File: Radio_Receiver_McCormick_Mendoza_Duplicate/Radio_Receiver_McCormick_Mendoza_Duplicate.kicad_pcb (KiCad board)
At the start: 4 copper layers, 100 x 100 mm, 244 parts, among them J1 VBAT, J10 CLK_2, J11 I_LO, J12 Q_LO, J13 I_0, J14 I_180, J15 Q_90, J16 Q_270, J17 I_RAW, J18 Conn_01x02_Female, J19 Conn_01x02_Female, J2 GND, J20 Q_RAW, J21 SDR Out, J23 VDDA, J24 CLK_0, J25 OLED, J26 +5V, J28 Conn_01x01_Pin, J3 VA_3.3, J33 XFIL_IN, J34 XFIL_OUT, J35 3.5mm_Jack, J36 +5V RAW, J37 V_4.5, J38 DAC_FLT, J39 VDD, J4 VA_4.5, J40 DAC_FMT, J41 V_DIV, J42 VDDA/2, J45 CENTER_TAP, J46 3.5mm_Jack, J47 FIL_IN, J5 Conn_Coaxial, J6 Conn_01x02, J7 Micro_SD-TF_PUSH, J8 FIL_OUT, J9 CLK_1, SW1 RotaryEncoder_Switch_MP, SW6 09.03290.01, T1 Transformer_1P_SS, U1 TPS7A2045PDQN, U10 OPA1612AID, U11 INA821ID, U12 PCM1808PWR, U13 SN74CBT3253CDBR, U14 PCM5102A, U2 TPS7A2045PDQN, U3 TPS72733DSER, U4 Pico, U5 Si5351A-B-GT, U6 SN74AC74DR, U8 SN74CBT3253CDBR, U9 INA821ID, Y1 ASTX-H11-24.576MHZ-T

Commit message: Added comment
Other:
- board text added: "These is clustered by groups as shown in the Schematics. NOT FINISHED"
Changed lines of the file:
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@@
 		(layer "User.4")
+	)
+	(gr_text "These is clustered by groups as shown in the Schematics. \nNOT FINISHED\n"
+		(at -138 111.5 0)
+		(layer "F.Cu")
+		(effects
+			(font
+				(size 1.5 1.5)
+				(thickness 0.3)
+				(bold yes)
+			)
+			(justify left bottom)
+		)
 	)
 	(gr_text "Analog"

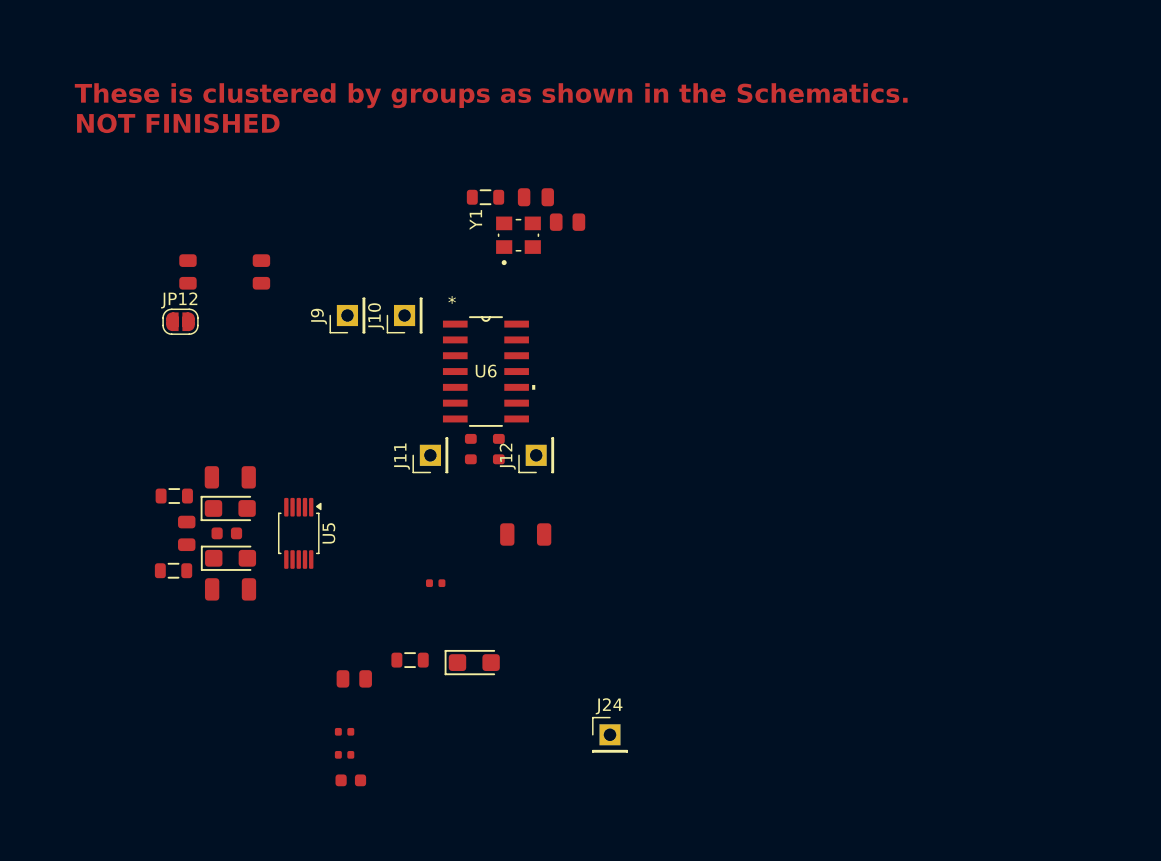
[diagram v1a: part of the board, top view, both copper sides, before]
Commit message: Fixed the clock and johnson counter
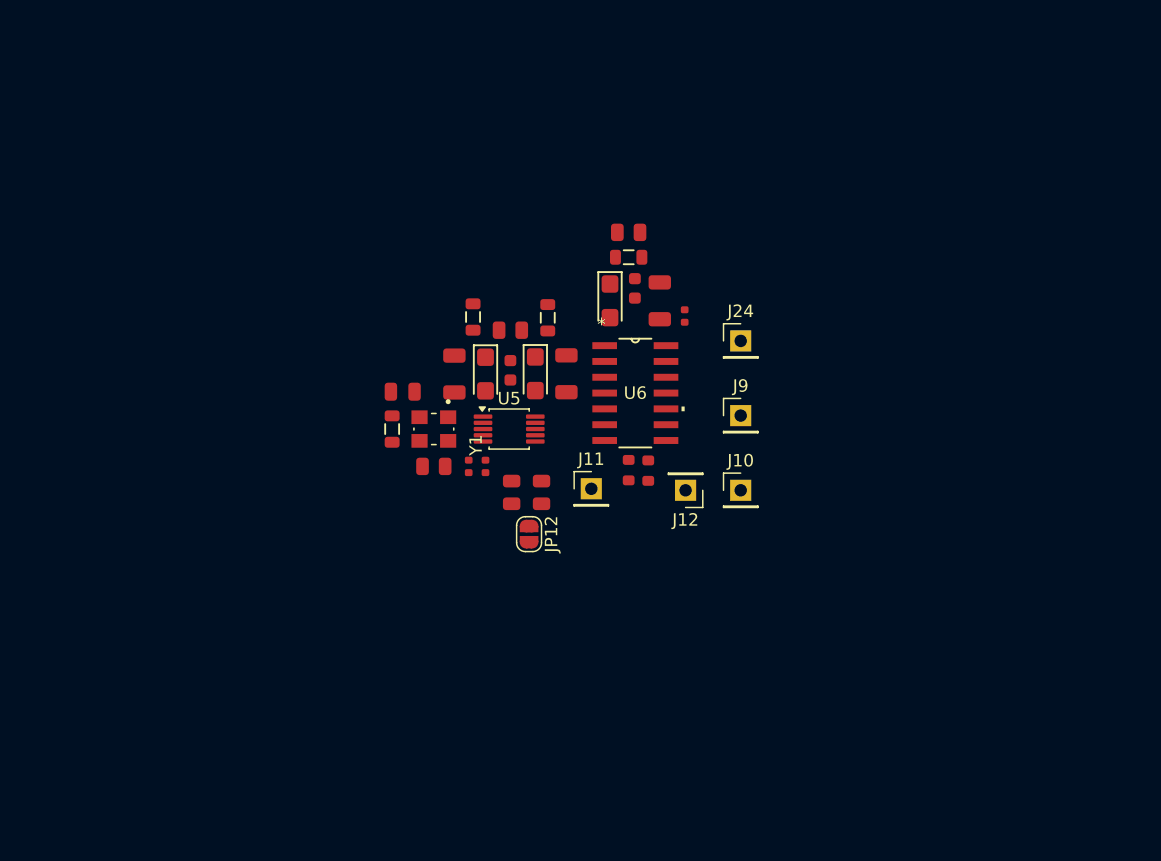
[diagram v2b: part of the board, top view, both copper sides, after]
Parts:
- moved C70 45.6 mm to (-93.0, 123.8), turned to -90 degrees
- moved R41 42.1 mm to (-93.5, 119.3)
- moved FB13 36.8 mm to (-93.5, 121.3)
- moved J24 33.3 mm to (-84.5, 128.0)
- moved FB15 33.2 mm to (-100.0, 126.2), turned to -90 degrees
- moved JP12 32.8 mm to (-101.5, 143.6), turned to -90 degrees
- moved J9 32.6 mm to (-84.5, 134.0), turned to 0 degrees
- moved FB16 31.5 mm to (-106.0, 126.1), turned to -90 degrees
- moved R36 31.5 mm to (-102.9, 140.2)
- moved C71 31.0 mm to (-95.0, 124.8), turned to -90 degrees
- moved R4 30.7 mm to (-103.0, 127.2), turned to 180 degrees
- moved J10 30.4 mm to (-84.5, 140.0), turned to 0 degrees
- moved C8 29.3 mm to (-89.0, 126.0), turned to 90 degrees
- moved R34 28.6 mm to (-100.5, 140.2)
- moved C77 28.3 mm to (-98.5, 130.7), turned to -90 degrees
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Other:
- board text removed: "These is clustered by groups as shown in the Schematics. NOT FINISHED"

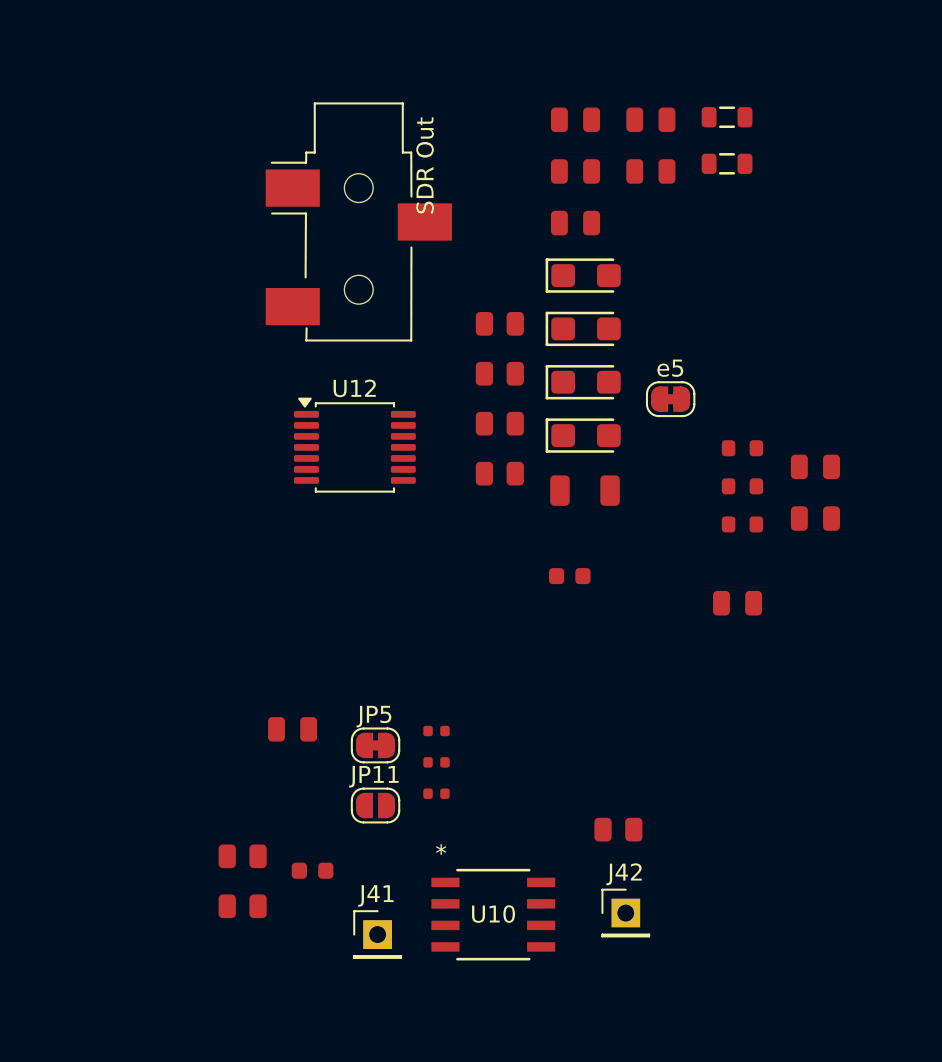
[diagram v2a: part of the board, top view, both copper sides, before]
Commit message: ADC finished
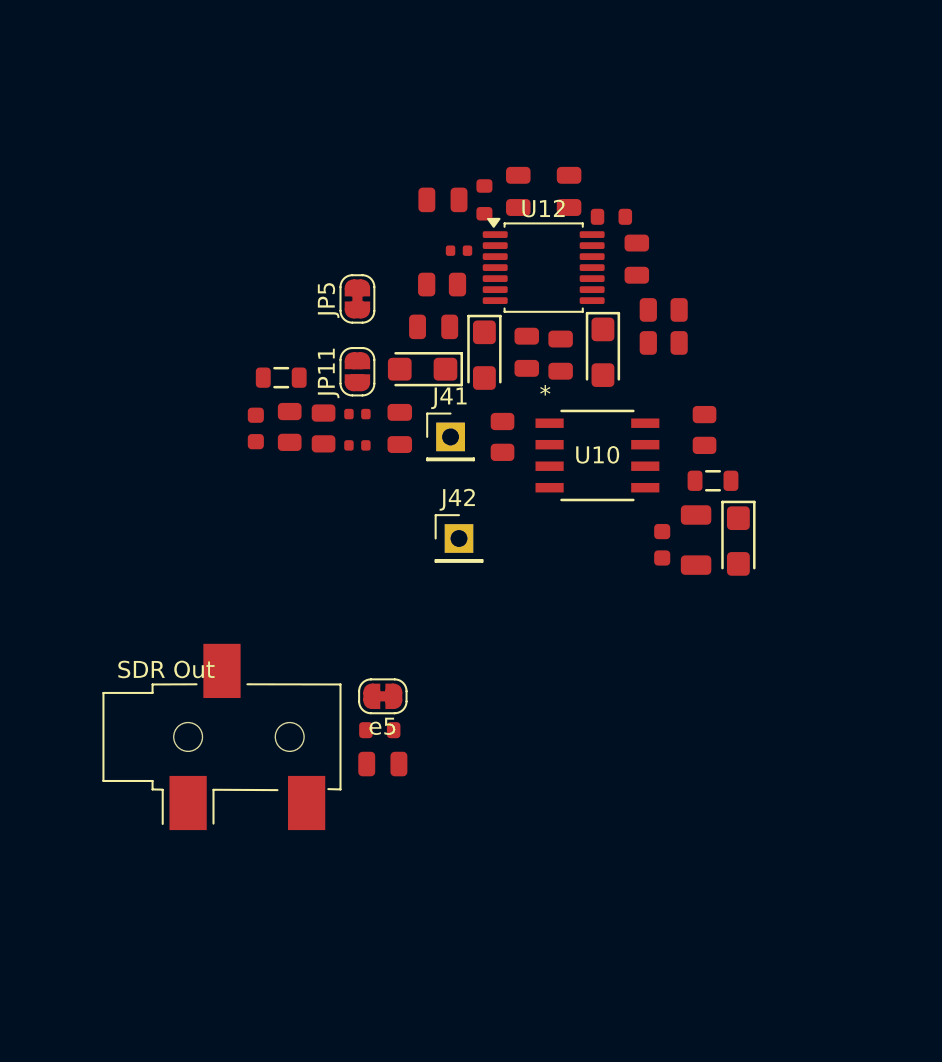
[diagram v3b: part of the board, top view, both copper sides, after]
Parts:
- moved R3 32.1 mm to (-25.0, 193.2), turned to 180 degrees
- moved J41 29.7 mm to (-25.5, 204.2)
- moved FB21 29.2 mm to (-35.5, 200.7)
- moved J21 29.1 mm to (-37.0, 221.9), turned to 90 degrees
- moved R53 28.6 mm to (-33.0, 203.7), turned to -90 degrees
- moved U10 27.8 mm to (-16.8, 205.3)
- moved C23 27.1 mm to (-25.9, 190.2), turned to 180 degrees
- moved JP5 26.4 mm to (-31.0, 196.0), turned to 90 degrees
- moved C93 26.3 mm to (-37.0, 203.7), turned to -90 degrees
- moved JP11 25.6 mm to (-31.0, 200.3), turned to 90 degrees
- moved R52 25.5 mm to (-35.0, 203.6), turned to -90 degrees
- moved R31 24.6 mm to (-29.7, 221.5)
- moved e5 24.4 mm to (-29.5, 219.5), turned to 180 degrees
- moved J42 24.2 mm to (-25.0, 210.2)
- moved R5 24.2 mm to (-22.4, 204.2), turned to 90 degrees
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
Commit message: Started adding traces
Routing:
- net GND: track 0.00 -> 78.4 mm
- net V_DIV: track 0.00 -> 12.0 mm
- net Net-(U12-VREF): track 0.00 -> 10.2 mm
- net Net-(JP11-B): track 0.00 -> 7.53 mm
- net Net-(JP5-B): track 0.00 -> 6.41 mm
- net Net-(U12-LRCK): track 0.00 -> 2.62 mm
- net Net-(C47-Pad1): track 0.00 -> 2.53 mm
- net Net-(U12-VINL): track 0.00 -> 1.84 mm
